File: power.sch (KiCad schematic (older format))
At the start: 20 parts, among them J201 Power_Planes, Q201 Q_PMOS_GSD, U201 TLV75733PDRV

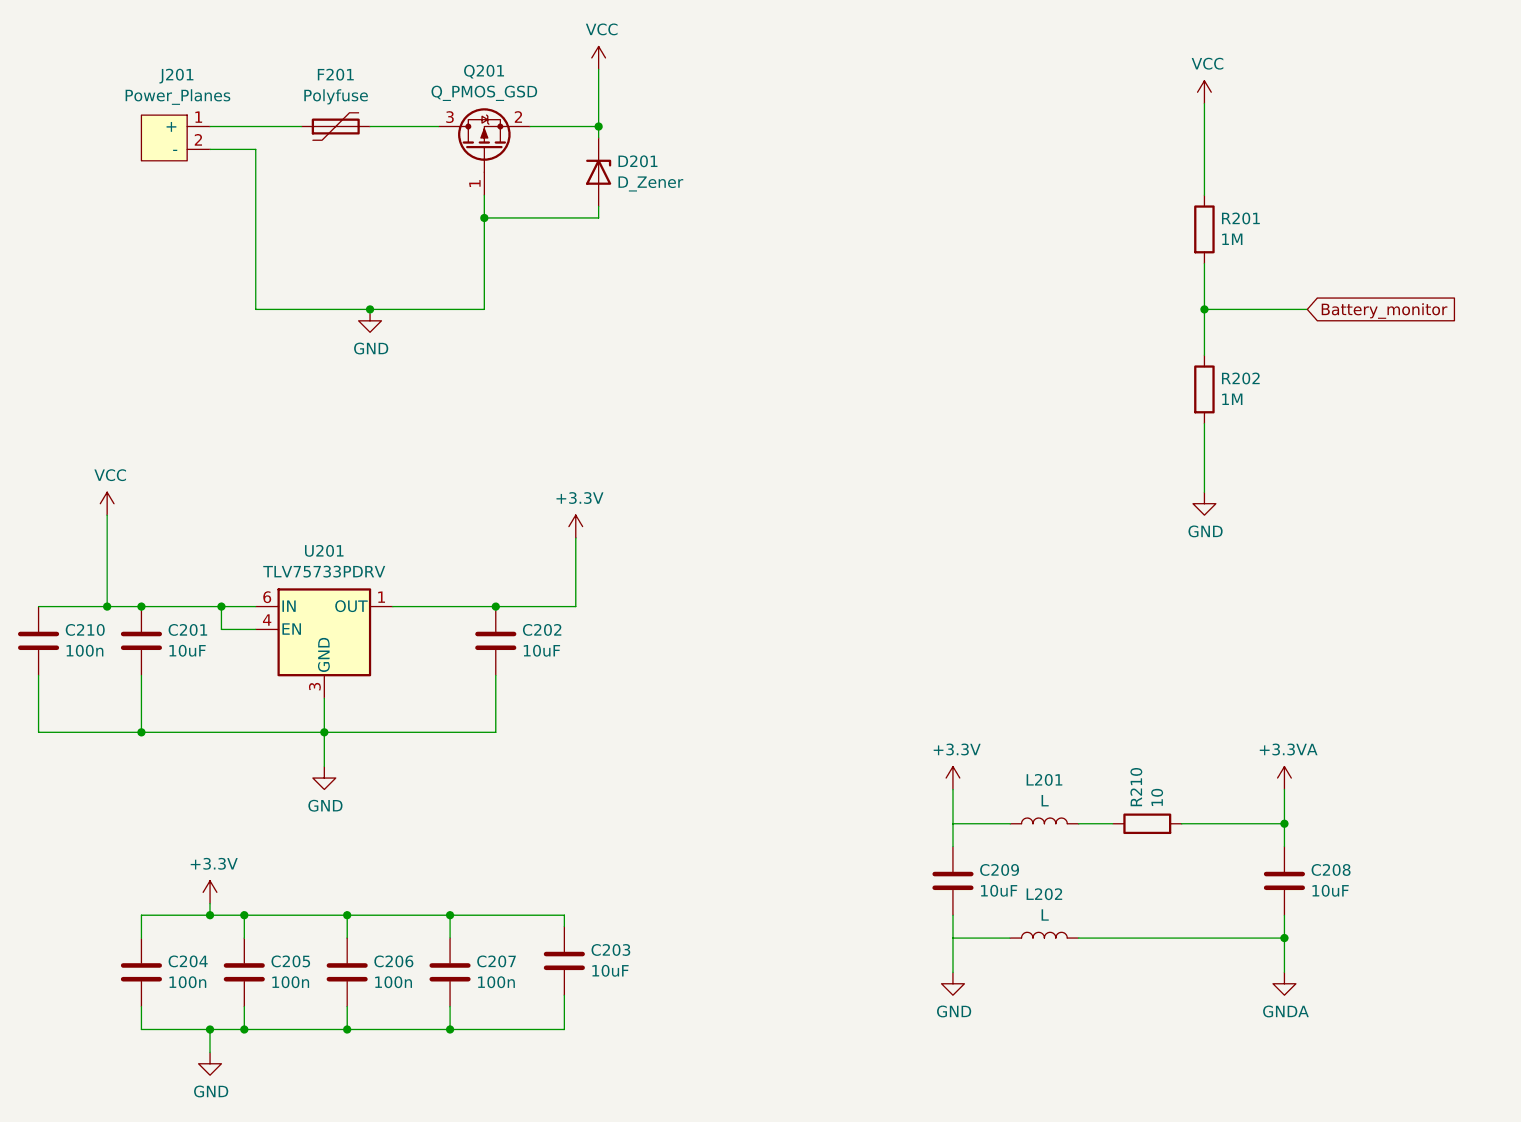
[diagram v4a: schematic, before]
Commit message: Updated to kicad 6. Added AMS1117 regulator. Did more layout work in power section.
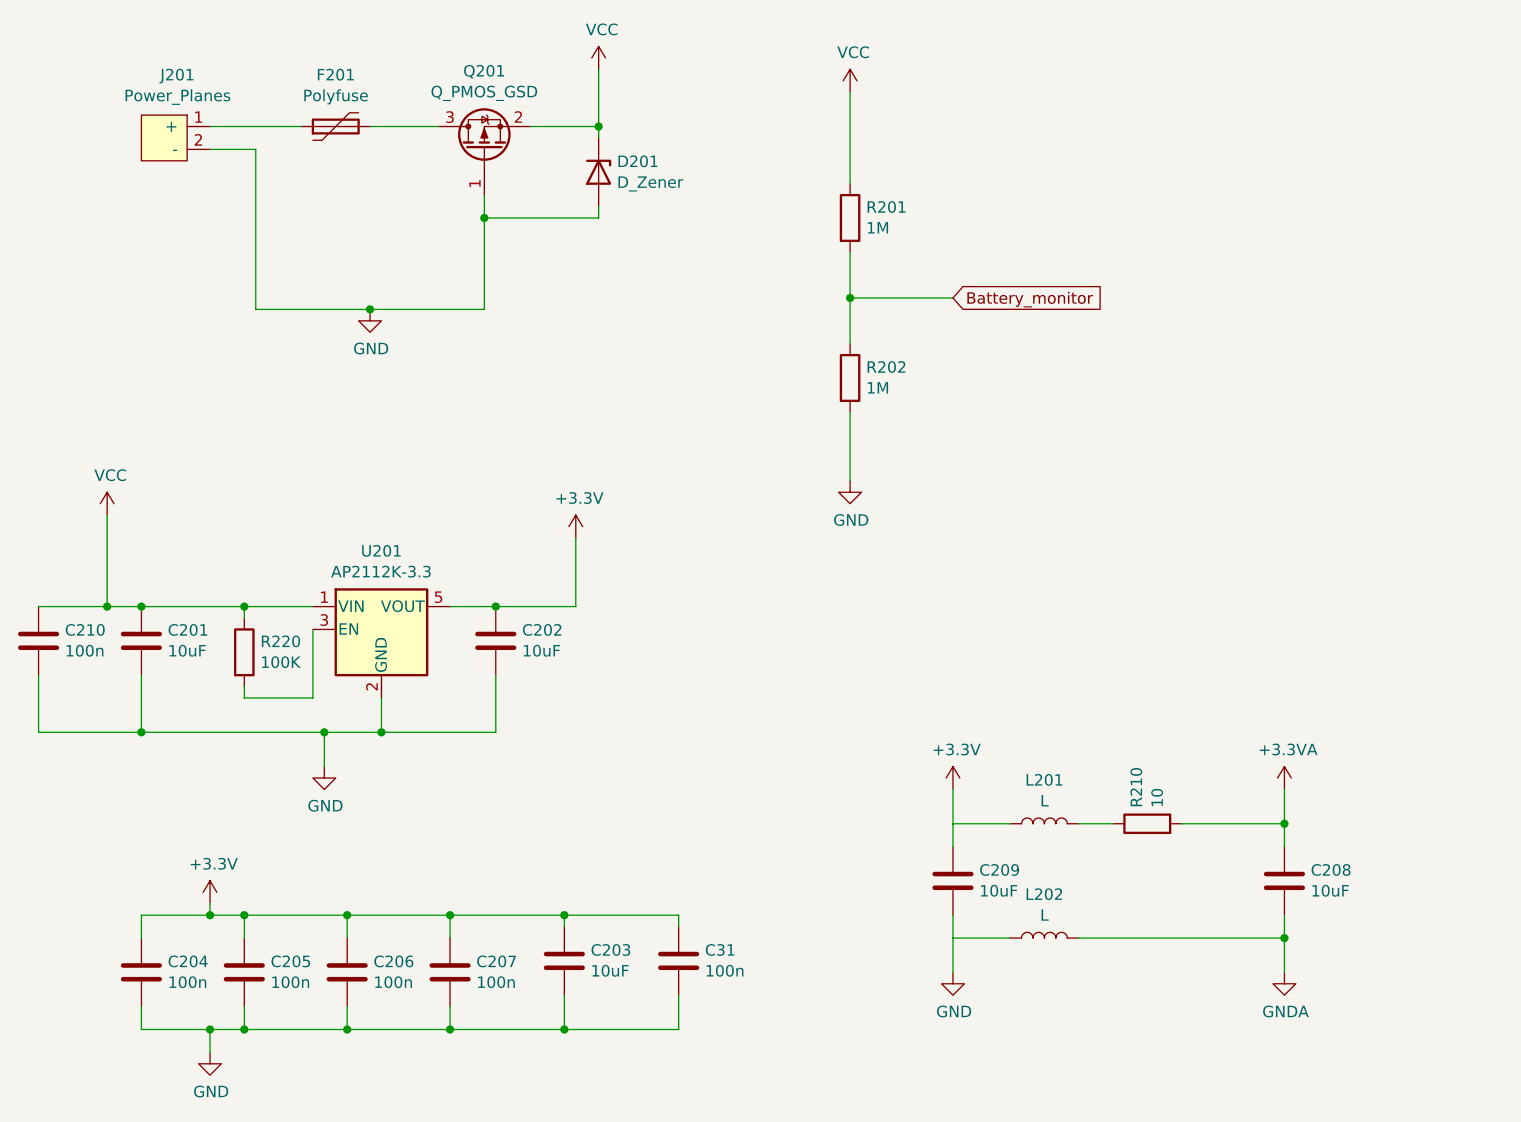
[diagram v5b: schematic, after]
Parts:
- removed U201: TLV75733PDRV, Package_SON:WSON-6-1EP_2x2mm_P0.65mm_EP1x1.6mm, symbol Regulator_Linear:TLV75733PDRV
- added C31: 100n, Capacitor_SMD:C_0603_1608Metric_Pad1.08x0.95mm_HandSolder, symbol Device:C
- added R220: 100K, Resistor_SMD:R_0603_1608Metric_Pad0.98x0.95mm_HandSolder, symbol Device:R
- added U201: AP2112K-3.3, Package_TO_SOT_SMD:SOT-23-5, symbol Regulator_Linear:AP2112K-3.3
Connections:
- net +3V3: now also C31.1, U201.5 (VOUT)
- net GND: now also C31.2, U201.2 (GND)
- net VCC: now also R220.1, U201.1 (VIN)
- new net: R220.2, U201.3 (EN)
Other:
- moved on the sheet: R201, R202
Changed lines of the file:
@@
 Connection ~ 2750 2000
-$Comp
-L Regulator_Linear:TLV75733PDRV U201
-U 1 1 61410663
-P 2550 3400
-F 0 "U201" H 2550 3742 50  0000 C CNN
-F 1 "TLV75733PDRV" H 2550 3651 50  0000 C CNN
-F 2 "Package_SON:WSON-6-1EP_2x2mm_P0.65mm_EP1x1.6mm" H 2550 3725 50  0001 C CIN
-F 3 "https://www.ti.com/lit/ds/symlink/tlv757p.pdf" H 2550 3450 50  0001 C CNN
-	1    2550 3400
-	1    0    0    -1
-$EndComp
 $Comp
 L power:+3.3V #PWR0118
@@
 $EndComp
 Wire Wire Line
-	2850 3300 3300 3300
-Wire Wire Line
 	3650 3300 3650 3000
 Wire Wire Line
 	1600 2900 1600 3300
-Wire Wire Line
-	2250 3400 2100 3400
-Wire Wire Line
-	2100 3400 2100 3300
-Connection ~ 2100 3300
-Wire Wire Line
-	2100 3300 2250 3300
-Wire Wire Line
-	2550 3700 2550 3850
 $Comp
 L Device:R R201
 U 1 1 6141B73C
-P 6400 1650
-F 0 "R201" H 6470 1696 50  0000 L CNN
-F 1 "1M" H 6470 1605 50  0000 L CNN
-F 2 "Resistor_SMD:R_0603_1608Metric_Pad0.98x0.95mm_HandSolder" V 6330 1650 50  0001 C CNN
-F 3 "~" H 6400 1650 50  0001 C CNN
-	1    6400 1650
+P 4850 1600
+F 0 "R201" H 4920 1646 50  0000 L CNN
+F 1 "1M" H 4920 1555 50  0000 L CNN
+F 2 "Resistor_SMD:R_0603_1608Metric_Pad0.98x0.95mm_HandSolder" V 4780 1600 50  0001 C CNN
+F 3 "~" H 4850 1600 50  0001 C CNN
+	1    4850 1600
 	1    0    0    -1
 $EndComp
@@
 L Device:R R202
 U 1 1 6141DF1C
-P 6400 2350
-F 0 "R202" H 6470 2396 50  0000 L CNN
-F 1 "1M" H 6470 2305 50  0000 L CNN
-F 2 "Resistor_SMD:R_0603_1608Metric_Pad0.98x0.95mm_HandSolder" V 6330 2350 50  0001 C CNN
-F 3 "~" H 6400 2350 50  0001 C CNN
-	1    6400 2350
+P 4850 2300
+F 0 "R202" H 4920 2346 50  0000 L CNN
+F 1 "1M" H 4920 2255 50  0000 L CNN
+F 2 "Resistor_SMD:R_0603_1608Metric_Pad0.98x0.95mm_HandSolder" V 4780 2300 50  0001 C CNN
+F 3 "~" H 4850 2300 50  0001 C CNN
+	1    4850 2300
 	1    0    0    -1
 $EndComp
@@
 L power:VCC #PWR0121
 U 1 1 61420C16
-P 6400 1100
-F 0 "#PWR0121" H 6400 950 50  0001 C CNN
-F 1 "VCC" H 6415 1273 50  0000 C CNN
-F 2 "" H 6400 1100 50  0001 C CNN
-F 3 "" H 6400 1100 50  0001 C CNN
-	1    6400 1100
-	1    0    0    -1
-$EndComp
-Wire Wire Line
-	6400 1100 6400 1500
-Wire Wire Line
-	6400 1800 6400 2000
+P 4850 1050
+F 0 "#PWR0121" H 4850 900 50  0001 C CNN
+F 1 "VCC" H 4865 1223 50  0000 C CNN
+F 2 "" H 4850 1050 50  0001 C CNN
+F 3 "" H 4850 1050 50  0001 C CNN
+	1    4850 1050
+	1    0    0    -1
+$EndComp
+Wire Wire Line
+	4850 1050 4850 1450
+Wire Wire Line
+	4850 1750 4850 1950
 $Comp
 L power:GND #PWR0122
 U 1 1 614222F9
-P 6400 2800
-F 0 "#PWR0122" H 6400 2550 50  0001 C CNN
-F 1 "GND" H 6405 2627 50  0000 C CNN
-F 2 "" H 6400 2800 50  0001 C CNN
-F 3 "" H 6400 2800 50  0001 C CNN
-	1    6400 2800
-	1    0    0    -1
-$EndComp
-Wire Wire Line
-	6400 2500 6400 2800
-Text GLabel 6850 2000 2    50   Input ~ 0
+P 4850 2750
+F 0 "#PWR0122" H 4850 2500 50  0001 C CNN
+F 1 "GND" H 4855 2577 50  0000 C CNN
+F 2 "" H 4850 2750 50  0001 C CNN
+F 3 "" H 4850 2750 50  0001 C CNN
+	1    4850 2750
+	1    0    0    -1
+$EndComp
+Wire Wire Line
+	4850 2450 4850 2750
+Text GLabel 5300 1950 2    50   Input ~ 0
 Battery_monitor
 Wire Wire Line
-	6850 2000 6400 2000
-Connection ~ 6400 2000
-Wire Wire Line
-	6400 2000 6400 2200
+	5300 1950 4850 1950
+Connection ~ 4850 1950
+Wire Wire Line
+	4850 1950 4850 2150
 $Comp
 L Device:C C202
@@
 	1    0    0    -1
 $EndComp
-Connection ~ 3300 3300
 Wire Wire Line
 	3300 3300 3650 3300
@@
 	3300 3600 3300 3850
 Wire Wire Line
-	3300 3850 2550 3850
-Connection ~ 2550 3850
-Wire Wire Line
-	2550 3850 2550 4000
-Wire Wire Line
-	2550 3850 1750 3850
-Wire Wire Line
 	1750 3850 1750 3600
 Connection ~ 1750 3300
-Wire Wire Line
-	1750 3300 2100 3300
 $Comp
 L Device:C C203
@@
 	1300 3850 1750 3850
 Connection ~ 1750 3850
+Connection ~ 3300 3300
+Wire Wire Line
+	2550 3850 1750 3850
+Wire Wire Line
+	2550 3850 2550 4000
+Connection ~ 2550 3850
+Wire Wire Line
+	3300 3850 2800 3850
+Wire Wire Line
+	2800 3700 2800 3850
+$Comp
+L Device:R R220
+U 1 1 61AFC736
+P 2200 3500
+F 0 "R220" H 2270 3546 50  0000 L CNN
+F 1 "100K" H 2270 3455 50  0000 L CNN
+F 2 "Resistor_SMD:R_0603_1608Metric_Pad0.98x0.95mm_HandSolder" V 2130 3500 50  0001 C CNN
+F 3 "~" H 2200 3500 50  0001 C CNN
+	1    2200 3500
+	1    0    0    -1
+$EndComp
+Wire Wire Line
+	2200 3350 2200 3300
+Wire Wire Line
+	2500 3400 2500 3700
+Wire Wire Line
+	2200 3700 2200 3650
+Connection ~ 2800 3850
+Wire Wire Line
+	2800 3850 2550 3850
+Wire Wire Line
+	3100 3300 3300 3300
+$Comp
+L Regulator_Linear:AP2112K-3.3 U201
+U 1 1 61AEB8B2
+P 2800 3400
+F 0 "U201" H 2800 3742 50  0000 C CNN
+F 1 "AP2112K-3.3" H 2800 3651 50  0000 C CNN
+F 2 "Package_TO_SOT_SMD:SOT-23-5" H 2800 3725 50  0001 C CNN
+F 3 "https://www.diodes.com/assets/Datasheets/AP2112.pdf" H 2800 3500 50  0001 C CNN
+	1    2800 3400
+	1    0    0    -1
+$EndComp
+Connection ~ 2200 3300
+Wire Wire Line
+	1750 3300 2200 3300
+Wire Wire Line
+	2200 3300 2500 3300
+Wire Wire Line
+	2200 3700 2500 3700
+Wire Wire Line
+	4100 5000 4100 5150
+Wire Wire Line
+	3600 4650 4100 4650
+Wire Wire Line
+	4100 4650 4100 4700
+Connection ~ 3600 4650
+Wire Wire Line
+	4100 5150 3600 5150
+Connection ~ 3600 5150
+$Comp
+L Device:C C31
+U 1 1 61B54507
+P 4100 4850
+F 0 "C31" H 4215 4896 50  0000 L CNN
+F 1 "100n" H 4215 4805 50  0000 L CNN
+F 2 "Capacitor_SMD:C_0603_1608Metric_Pad1.08x0.95mm_HandSolder" H 4138 4700 50  0001 C CNN
+F 3 "~" H 4100 4850 50  0001 C CNN
+	1    4100 4850
+	1    0    0    -1
+$EndComp
 $EndSCHEMATC
